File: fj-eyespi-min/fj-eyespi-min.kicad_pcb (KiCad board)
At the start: 2 copper layers, 45.6 x 24.7 mm, 2 parts, among them J1 Conn_01x18_Socket, J2 Conn_02x16_Odd_Even

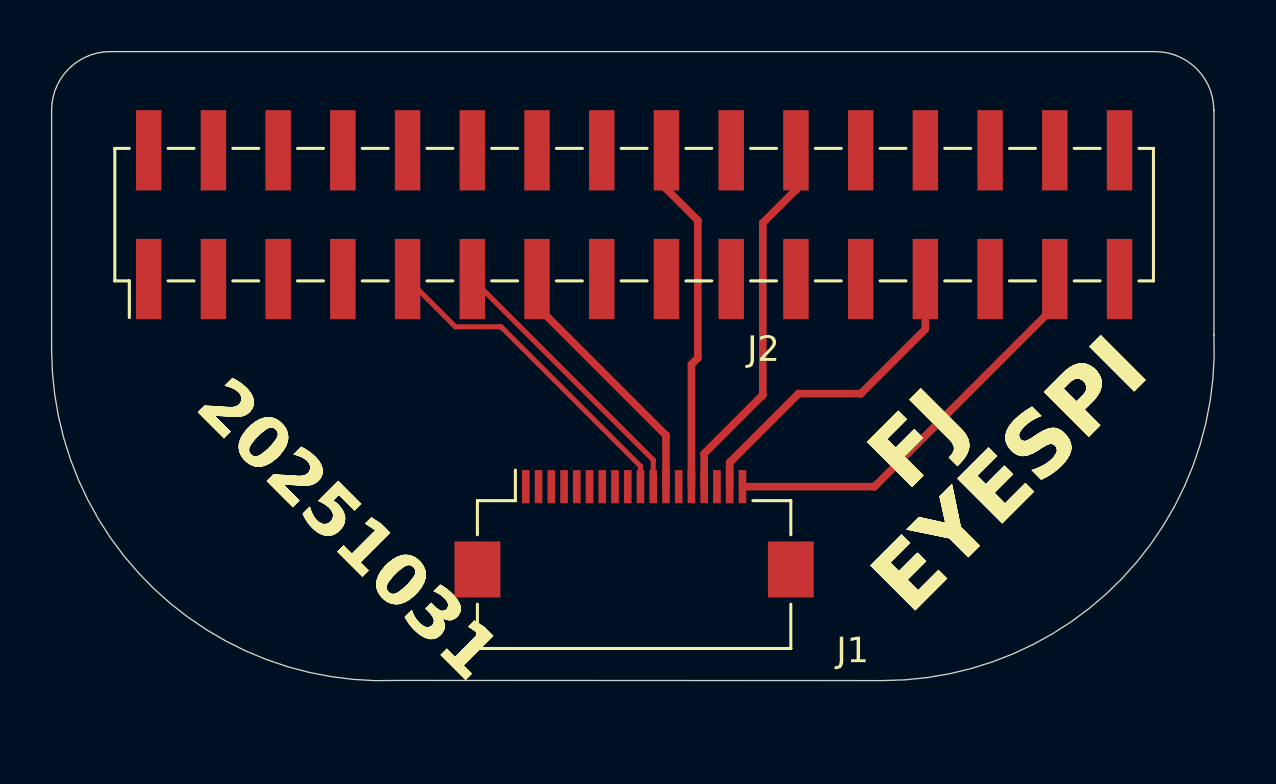
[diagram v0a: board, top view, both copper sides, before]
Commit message: total remix
min and max boards re-routed and date, new silks....
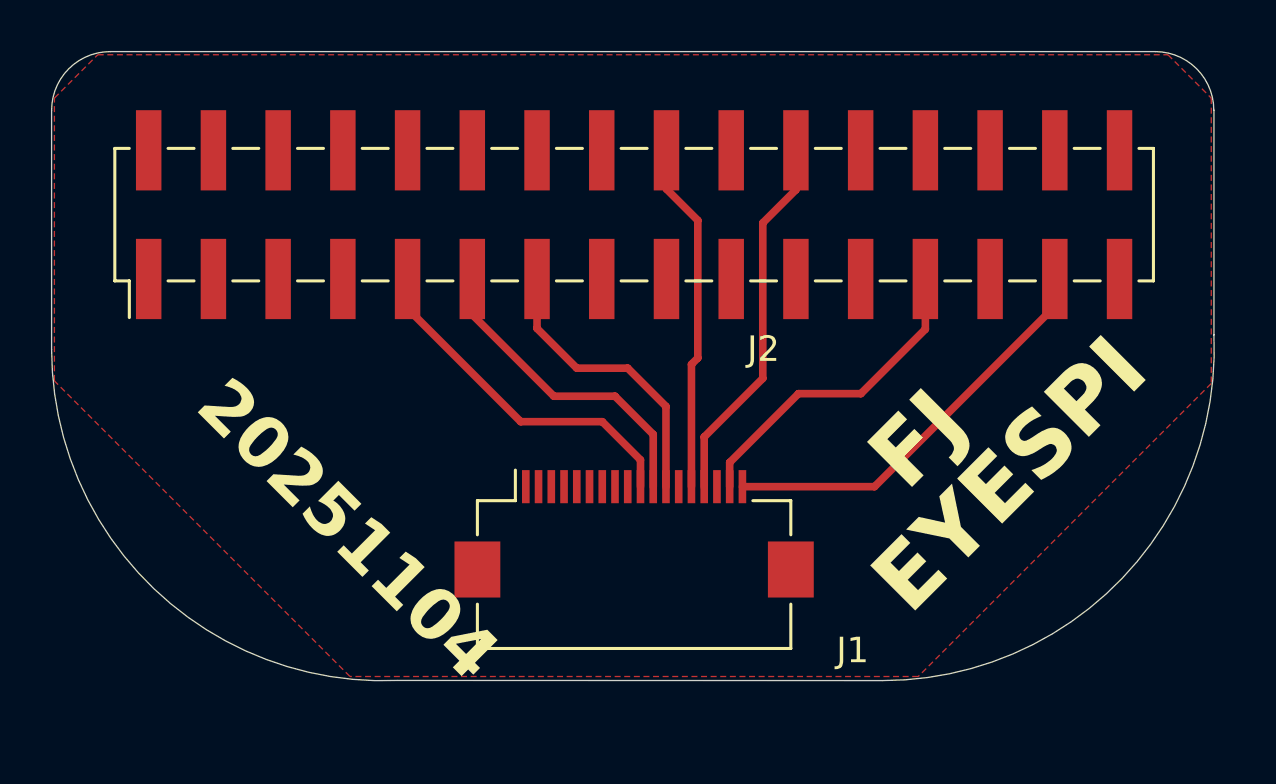
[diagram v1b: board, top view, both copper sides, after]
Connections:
- J2 pad 1: +5V -> unconnected-(J2-Pin_1-Pad1)
- J2 pad 2: +5V -> unconnected-(J2-Pin_2-Pad2)
- J2 pad 3: 3v3 -> unconnected-(J2-Pin_3-Pad3)
- J2 pad 30: 3v3 -> unconnected-(J2-Pin_30-Pad30)
- J2 pad 31: +5V -> unconnected-(J2-Pin_31-Pad31)
- J2 pad 32: +5V -> unconnected-(J2-Pin_32-Pad32)
- J2 pad 4: 3v3 -> unconnected-(J2-Pin_4-Pad4)
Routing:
- net /rst: track 11.1 -> 12.5 mm
- net /dc: track 10.2 -> 11.4 mm
- net /tcs: track 13.0 -> 13.8 mm
- added copper zone on F.Cu, net gnd
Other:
- board text added: "20251104"
- board text added: "Fruit Jam EYESPI MIN 20251104"
- board text removed: "20251031"
